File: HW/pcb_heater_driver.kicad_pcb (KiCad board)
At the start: 2 copper layers, 158 x 102.5 mm, 69 parts, among them J1 Heater, J2 JTAG, J3 USB_C_Receptacle_USB2.0, J4 USB_C_Receptacle_USB2.0, Q1 RQ3E110AJ, Q2 BC817, Q3 BC817, SW1 SW_SPST, SW2 SW_DPST, SW3 SW_DPST, SW4 SW_SPST, SW5 SW_SPST, U1 ESP32-S2-MINI-2, U2 TS30042-M000QFNR, U3 CH340C

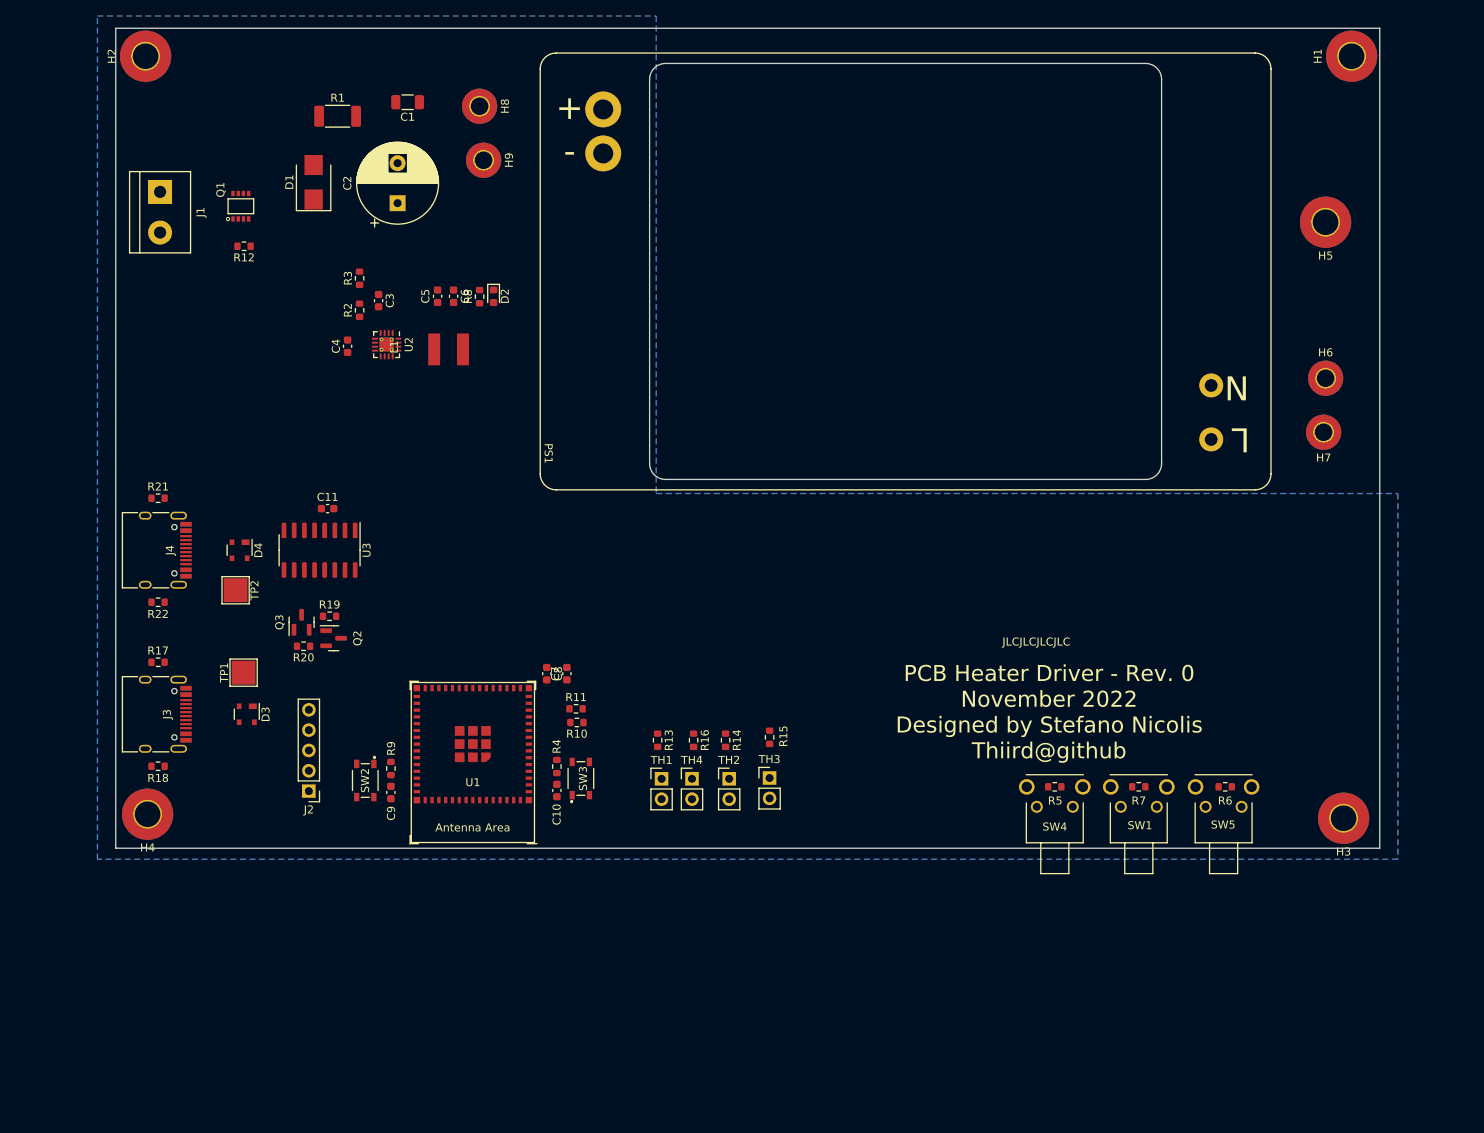
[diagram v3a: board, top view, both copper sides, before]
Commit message: Work on layout, sch fixes, added several 3d models
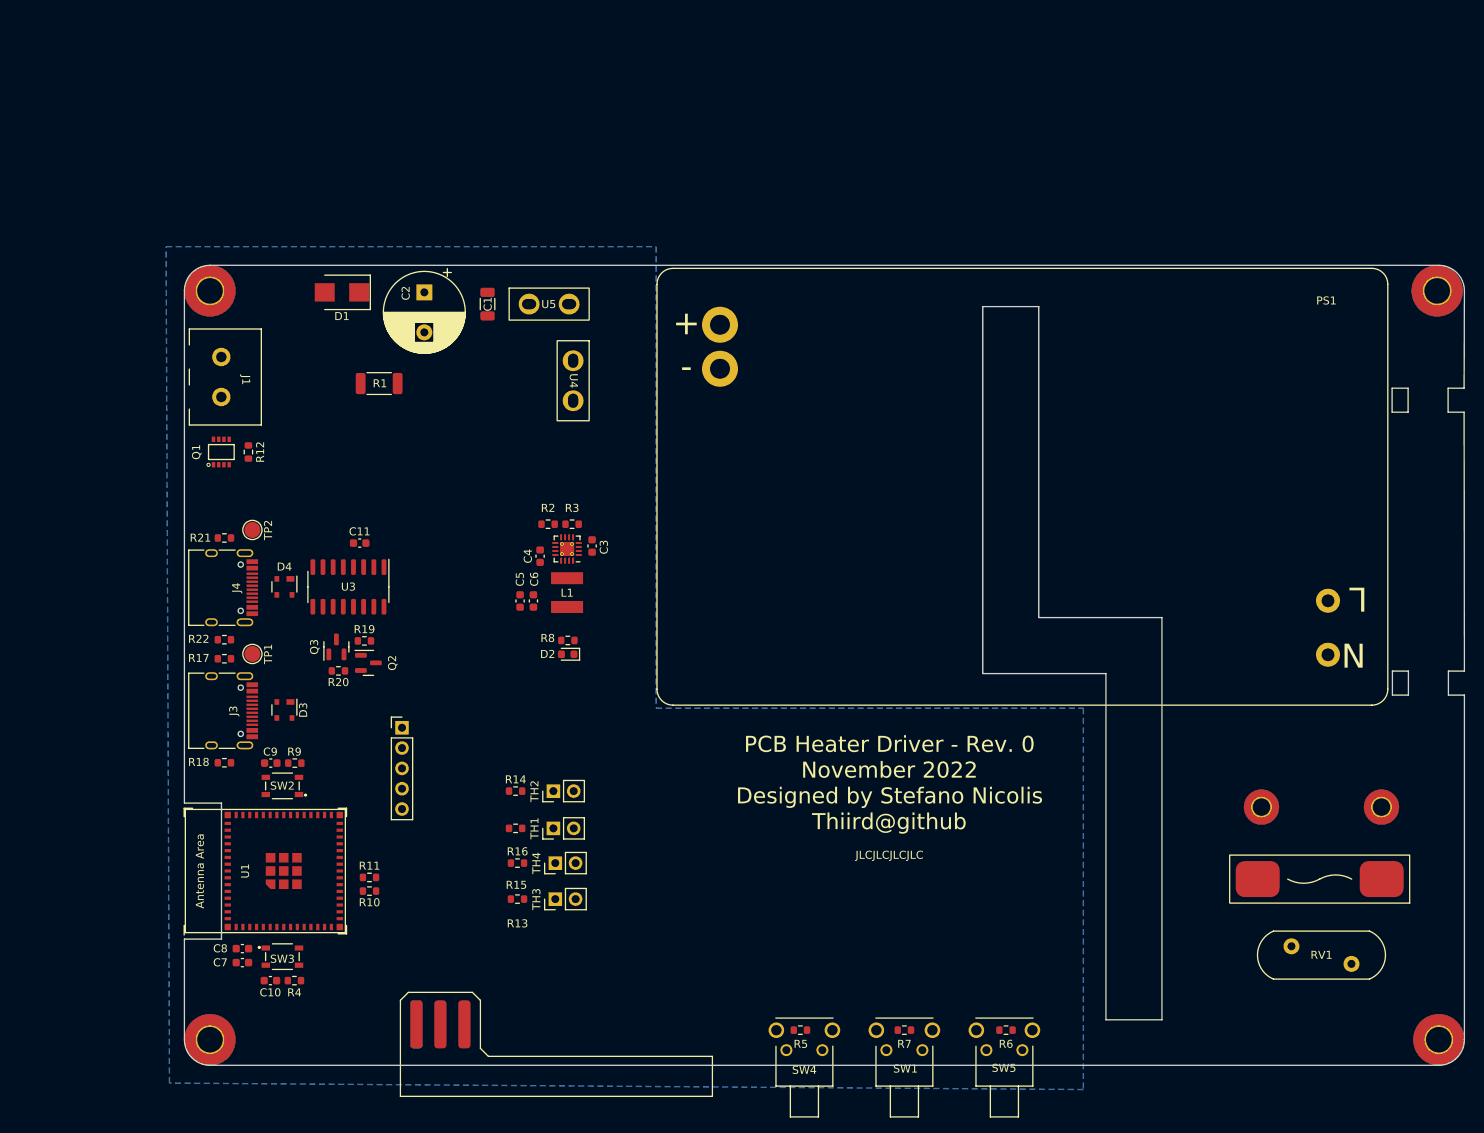
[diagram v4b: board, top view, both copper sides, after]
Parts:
- removed H5: AC_cable_fixture, MountingHole:MountingHole_3.2mm_M3_Pad_TopBottom
- removed H8, H9: AC_LIVE, MountingHole:MountingHole_2.2mm_M2_Pad_TopBottom
- added F1: Fuse, 3622_fuse_holder:3622, F.Cu at (215.0, 121.9)
- added J5: OLED, oled_angled:oled_angled, F.Cu at (102.1, 140.0)
- added RV1: Varistor, B72214S0351K101:B72214S0351K101, F.Cu at (215.2, 131.4)
- added U4: fork_p5.0mm, fork_connector_p5.0mm:fork_p5.0mm, F.Cu at (121.7, 59.6)
- added U5: fork_p5.0mm, fork_connector_p5.0mm:fork_p5.0mm, F.Cu at (118.7, 50.0)
- J1: footprint TerminalBlock:TerminalBlock_bornier-2_P5.08mm -> WR_TBL_Series_101:WR_TBL_Series_101
- R11: value TBD -> 37k
- R3: value 3750 -> 37k
- R4, R9: value 1k -> 22k
- TP1, TP2: footprint TestPoint:TestPoint_Pad_3.0x3.0mm -> TestPoint:TestPoint_Pad_D2.0mm
- moved C7 54.3 mm to (80.4, 132.3), turned to 0 degrees
- moved H6 54.1 mm to (222.7, 112.9), turned to 180 degrees
- moved C8 51.3 mm to (80.4, 130.5), turned to 180 degrees
- moved H7 47.5 mm to (207.7, 112.9), turned to 0 degrees
- moved D2 45.7 mm to (121.0, 93.8), turned to 180 degrees
- moved R8 44.4 mm to (121.0, 92.0), turned to 0 degrees
- moved R5 44.0 mm to (150.1, 140.7)
- moved SW4 43.6 mm to (150.6, 143.2)
- moved SW3 43.4 mm to (85.4, 131.5), turned to 0 degrees
- moved C10 43.0 mm to (83.9, 134.5), turned to 180 degrees
- moved R4 42.3 mm to (86.9, 134.5), turned to 180 degrees
- moved R7 42.2 mm to (163.1, 140.7)
- moved SW1 42.2 mm to (163.1, 143.2)
- moved SW5 40.9 mm to (175.6, 143.2)
- moved R6 40.9 mm to (175.8, 140.7)
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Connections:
- net heater_LOW renamed /Heater/heater_LOW
- C1 pad 1: Net-(C1-Pad1) -> +12V
- C2 pad 1: Net-(C1-Pad1) -> +12V
- D1 pad 1: Net-(C1-Pad1) -> +12V
- D3 pad 4: +3V3 -> unconnected-(D3-Pad4)
- D4 pad 4: +3V3 -> unconnected-(D4-Pad4)
- PS1 pad 4: Net-(C1-Pad1) -> Net-(PS1-Pad4)
- R1 pad 1: Net-(C1-Pad1) -> +12V
- U1 pad 11: unconnected-(U1-Pad11) -> temperature_plus
- U1 pad 12: unconnected-(U1-Pad12) -> temperature_minus
- U1 pad 13: unconnected-(U1-Pad13) -> user_action
- U1 pad 14: temp_heater_1 -> temp_heater_3
- U1 pad 15: temp_heater_2 -> temp_mosfet
- U1 pad 16: temp_heater_3 -> unconnected-(U1-Pad16)
- U1 pad 17: temp_mosfet -> unconnected-(U1-Pad17)
- U1 pad 20: unconnected-(U1-Pad20) -> current_sense_LOW
- U1 pad 25: unconnected-(U1-Pad25) -> temp_heater_1
- U1 pad 26: unconnected-(U1-Pad26) -> temp_heater_2
- U1 pad 32: user_action -> unconnected-(U1-Pad32)
- U1 pad 33: temperature_minus -> unconnected-(U1-Pad33)
- U1 pad 34: temperature_plus -> unconnected-(U1-Pad34)
- U1 pad 6: current_sense_LOW -> unconnected-(U1-Pad6)
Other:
- board size 158 x 102.5 mm -> 160 x 100 mm

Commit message: starterd routing, removed OTG usb port
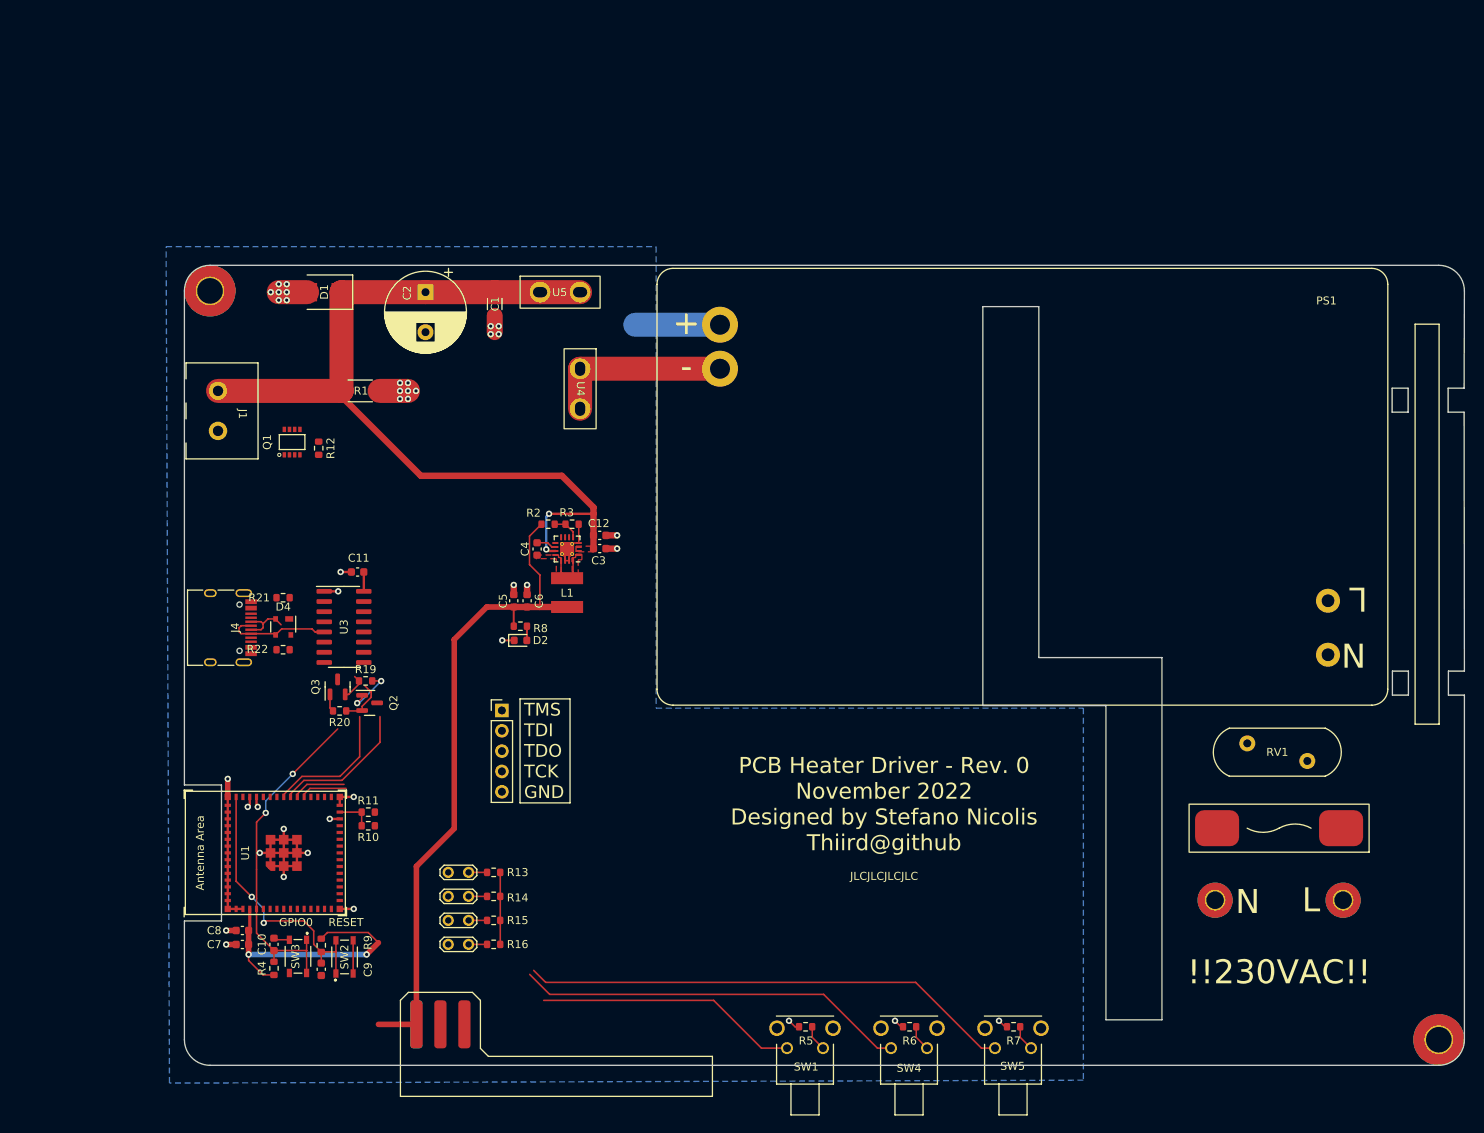
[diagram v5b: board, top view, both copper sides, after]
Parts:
- removed D3: PRTR5V0U2X, Package_TO_SOT_SMD:SOT-143
- removed H1: MH2, MountingHole:MountingHole_3.2mm_M3_Pad_TopBottom
- removed H4: MH4, MountingHole:MountingHole_3.2mm_M3_Pad_TopBottom
- removed J3: USB_C_Receptacle_USB2.0, Connector_USB:USB_C_Receptacle_HRO_TYPE-C-31-M-12
- removed R17, R18: 5k1, Resistor_SMD:R_0603_1608Metric
- removed TP1, TP2: TestPoint, TestPoint:TestPoint_Pad_D2.0mm
- added C12: 100n, Capacitor_SMD:C_0603_1608Metric, F.Cu at (125.0, 78.9)
- TH1, TH2, TH3, TH4: footprint Connector_PinHeader_2.54mm:PinHeader_1x02_P2.54mm_Vertical -> TestPoint:TestPoint_2Pads_Pitch2.54mm_Drill0.8mm
- moved C9 26.5 mm to (90.2, 133.1), turned to -90 degrees
- moved RV1 26.0 mm to (209.7, 106.0)
- moved R9 23.0 mm to (90.2, 130.1), turned to -90 degrees
- moved SW2 22.8 mm to (93.1, 131.6), turned to 90 degrees
- moved TH2 18.6 mm to (106.1, 124.0), turned to 0 degrees
- moved TH4 16.8 mm to (106.1, 130.0), turned to 0 degrees
- moved TH1 14.2 mm to (106.1, 121.0), turned to 0 degrees
- moved R7 13.7 mm to (176.8, 140.3)
- moved TH3 13.6 mm to (106.1, 127.0), turned to 0 degrees
- moved R14 13.4 mm to (111.8, 124.0), turned to 180 degrees
- moved SW4 13.1 mm to (163.7, 143.0)
- moved H7 13.0 mm to (201.9, 124.5), turned to 180 degrees
- moved J2 12.7 mm to (112.8, 100.8)
- moved H6 12.6 mm to (217.9, 124.5), turned to 0 degrees
- moved SW1 12.4 mm to (150.7, 143.0)
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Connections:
- C5 pad 1: /Power/PGND -> GND
- C6 pad 1: /Power/PGND -> GND
- D4 pad 2: /Peripherals/UART_USB_D+ -> /Peripherals/UART_USB_D-
- D4 pad 3: /Peripherals/UART_USB_D- -> /Peripherals/UART_USB_D+
- J4 pad A4: +5V -> unconnected-(J4-PadA4)
- J4 pad A9: +5V -> unconnected-(J4-PadA4)
- J4 pad B4: +5V -> unconnected-(J4-PadA4)
- J4 pad B9: +5V -> unconnected-(J4-PadA4)
- J5 pad 1: SDA -> GND
- J5 pad 2: SCL -> +3V3
- J5 pad 3: +3V3 -> SCL
- J5 pad 4: GND -> SDA
- U1 pad 10: unconnected-(U1-Pad10) -> user_action
- U1 pad 13: user_action -> unconnected-(U1-Pad13)
- U1 pad 14: temp_heater_3 -> unconnected-(U1-Pad14)
- U1 pad 15: temp_mosfet -> unconnected-(U1-Pad15)
- U1 pad 16: unconnected-(U1-Pad16) -> SCL
- U1 pad 17: unconnected-(U1-Pad17) -> SDA
- U1 pad 2: Net-(U1-Pad2) -> GND
- U1 pad 20: current_sense_LOW -> unconnected-(U1-Pad20)
- U1 pad 25: temp_heater_1 -> unconnected-(U1-Pad25)
- U1 pad 26: temp_heater_2 -> temp_mosfet
- U1 pad 28: SDA -> GND
- U1 pad 29: SCL -> current_sense_LOW
- U1 pad 30: Net-(U1-Pad2) -> GND
- U1 pad 31: unconnected-(U1-Pad31) -> temp_heater_3
- U1 pad 32: unconnected-(U1-Pad32) -> temp_heater_2
- U1 pad 33: unconnected-(U1-Pad33) -> temp_heater_1
- U1 pad 34: unconnected-(U1-Pad34) -> mosfet_gate
- U1 pad 42: Net-(U1-Pad2) -> GND
- U1 pad 43: Net-(U1-Pad2) -> GND
- U1 pad 46: Net-(U1-Pad2) -> GND
- U1 pad 47: Net-(U1-Pad2) -> GND
- U1 pad 48: Net-(U1-Pad2) -> GND
- U1 pad 49: Net-(U1-Pad2) -> GND
- U1 pad 50: Net-(U1-Pad2) -> GND
- U1 pad 51: Net-(U1-Pad2) -> GND
- U1 pad 52: Net-(U1-Pad2) -> GND
- U1 pad 53: Net-(U1-Pad2) -> GND
- U1 pad 54: Net-(U1-Pad2) -> GND
- U1 pad 55: Net-(U1-Pad2) -> GND
- U1 pad 56: Net-(U1-Pad2) -> GND
- U1 pad 57: Net-(U1-Pad2) -> GND
- U1 pad 58: Net-(U1-Pad2) -> GND
- U1 pad 59: Net-(U1-Pad2) -> GND
- U1 pad 60: Net-(U1-Pad2) -> GND
- U1 pad 61: Net-(U1-Pad2) -> GND
- U1 pad 62: Net-(U1-Pad2) -> GND
- U1 pad 63: Net-(U1-Pad2) -> GND
- U1 pad 64: Net-(U1-Pad2) -> GND
- U1 pad 65: Net-(U1-Pad2) -> GND
- U2 pad 6: GND -> unconnected-(U2-Pad6)
- U2 pad 7: GND -> unconnected-(U2-Pad7)
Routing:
- net GND: track 0.00 -> 142.4 mm, vias 0 -> 42
- net +3V3: track 0.00 -> 131.3 mm, vias 0 -> 2
- net +12V: track 0.00 -> 112.1 mm, vias 0 -> 2
- net user_action: track 0.00 -> 61.7 mm
- net temperature_minus: track 0.00 -> 49.0 mm
- net RESET: track 0.00 -> 34.7 mm, vias 0 -> 2
- net temperature_plus: track 0.00 -> 32.9 mm
- net Net-(PS1-Pad4): track 0.00 -> 22.5 mm
- net /MCU/TDI: track 0.00 -> 17.5 mm
- net /MCU/TMS: track 0.00 -> 16.8 mm
- net /Peripherals/UART_USB_D+: track 0.00 -> 13.4 mm
- net /MCU/TDO: track 0.00 -> 6.69 mm
- net /Peripherals/UART_USB_D-: track 0.00 -> 6.54 mm
- net Net-(Q2-Pad1): track 0.00 -> 6.50 mm, vias 0 -> 2
- net /Peripherals/RTS: track 0.00 -> 5.89 mm
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- added copper zone on F.Cu, net +12V
- added copper zone on F.Cu, net Net-(C4-Pad2)
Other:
- outline, holes or cut-outs redrawn
- board text added: "!!230VAC!!"
- board text added: "GPIO0"
- board text added: "L"
- board text added: "N"
- board text added: "RESET"
- board text added: "TMS TDI TDO TCK GND"
